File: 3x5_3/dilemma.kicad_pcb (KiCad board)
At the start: 2 copper layers, 134.1 x 215.6 mm, 91 parts, among them J5001 BATTERY_CONN_DEANS, J5011 BATTERY_CONN_DEANS, SW101 NA_SW_Push, SW102 NA_SW_Push, SW103 NA_SW_Push, SW104 NA_SW_Push, SW105 NA_SW_Push, SW106 NA_SW_Push, SW107 NA_SW_Push, SW108 NA_SW_Push, SW109 NA_SW_Push, SW112 NA_SW_Push, SW113 NA_SW_Push, SW114 NA_SW_Push, SW115 NA_SW_Push, SW116 NA_SW_Push, SW117 NA_SW_Push, SW118 NA_SW_Push, SW119 NA_SW_Push, SW3001 NA_SW_Push, SW5002 NA_SW_Push, SW5003 NA_SW_Push, SW5004 NA_SW_Push, SW5005 NA_SW_Push, SW5006 NA_SW_Push, SW5007 NA_SW_Push, SW5008 NA_SW_Push, SW5009 NA_SW_Push, SW5010 NA_SW_Push, SW5011 NA_SW_Push, SW5012 NA_SW_Push, SW5013 NA_SW_Push, SW5014 NA_SW_Push, SW5015 NA_SW_Push, SW5016 NA_SW_Push, SW5017 NA_SW_Push, SW5018 NA_SW_Push, SW5019 NA_SW_Push, SW5021 SW_SPST, SW5022 SW_SPST, U5001 eliteC, U5007 eliteC

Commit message: add right side edge cuts
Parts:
- removed H101, H102, H104, H108: NA_M4, local-libraries:MountingHole_3mm_Pad_Via
- removed H111: NA_Mount, local-libraries:Tenting_Puck
- SW101, SW102, SW103, SW104, SW105, SW106, SW107, SW108, SW109, SW112, SW113, SW114, SW115, SW116, SW117, SW118, SW119, SW3001, SW5002, SW5003, SW5004, SW5005, SW5006, SW5007, SW5008, SW5009, SW5010, SW5011, SW5012, SW5013, SW5014, SW5015, SW5016, SW5017, SW5018, SW5019: footprint local-libraries:SW_Kailh_Choc_V2_1.00u -> local-libraries:SW_Kailh_Choc_V1V2_1.00u
- moved D115 152.3 mm to (59.8, 42.8), turned to 0 degrees
- moved D5038 148.0 mm to (65.6, 46.2), turned to 0 degrees
- moved D5034 143.9 mm to (59.8, 56.2), turned to 0 degrees
- moved D5046 135.7 mm to (71.4, 49.5), turned to 0 degrees
- moved D5045 134.7 mm to (71.4, 46.2), turned to 0 degrees
- moved D5044 118.1 mm to (71.4, 42.8), turned to 0 degrees
- moved D5043 115.8 mm to (71.4, 39.5), turned to 0 degrees
- moved D5042 115.0 mm to (65.6, 59.6), turned to 0 degrees
- moved D5039 103.6 mm to (65.6, 49.5), turned to 0 degrees
- moved D5041 103.3 mm to (65.6, 56.2), turned to 0 degrees
- moved D5040 102.7 mm to (65.6, 52.9), turned to 0 degrees
- moved D5035 90.3 mm to (59.8, 59.6), turned to 0 degrees
- moved D5037 89.5 mm to (65.6, 42.8), turned to 0 degrees
- moved D5033 77.0 mm to (59.8, 52.9), turned to 0 degrees
- moved D5032 75.6 mm to (59.8, 49.5), turned to 0 degrees
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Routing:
- net M_COL1: track 168.1 -> 0.00 mm, vias 1 -> 0
- net M_COL3: track 159.6 -> 0.00 mm, vias 1 -> 0
- net M_COL2: track 143.8 -> 0.00 mm, vias 1 -> 0
- net M_ROW4: track 137.9 -> 0.00 mm
- net M_ROW2: track 120.6 -> 0.00 mm
- net M_ROW1: track 113.2 -> 0.00 mm
- net M_ROW3: track 109.2 -> 0.00 mm
- net M_COL5: track 76.5 -> 0.00 mm, vias 1 -> 0
- net M_COL4: track 74.1 -> 0.00 mm, vias 1 -> 0
- net BAT: track 67.9 -> 0.00 mm
- net BAT_SW: track 30.1 -> 0.00 mm
- net Net-(D5041-A): track 22.4 -> 0.00 mm
- net Net-(D5032-A): track 20.6 -> 0.00 mm
- net Net-(D115-A): track 20.5 -> 0.00 mm
- net Net-(D112-A): track 20.4 -> 0.00 mm
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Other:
- board size 134.1 x 215.6 mm -> 273.1 x 220.6 mm

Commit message: left half edge cuts
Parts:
- removed D5001, D5002, D5003, D5004, D5005, D5006, D5007, D5008, D5009, D5010, D5011, D5012, D5013, D5014, D5015, D5016, D5017, D5018: D, Diode_SMD:D_SOD-123
- removed H5001, H5002, H5003, H5007: NA_M4, local-libraries:MountingHole_3mm_Pad_Via
- removed H5008: NA_Mount, local-libraries:Tenting_Puck
- moved D5038 153.4 mm to (203.7, 112.9), turned to 150 degrees
- moved D115 143.1 mm to (196.2, 85.9), turned to 180 degrees
- moved D5034 134.2 mm to (184.7, 105.2), turned to 165 degrees
- moved D5046 126.3 mm to (196.5, 66.7), turned to 180 degrees
- moved D5045 125.1 mm to (196.5, 47.7), turned to 180 degrees
- moved D5042 108.9 mm to (165.5, 102.9), turned to 180 degrees
- moved D5044 108.2 mm to (177.4, 64.4), turned to 180 degrees
- moved D5043 106.0 mm to (177.2, 45.2), turned to 180 degrees
- moved D5041 95.4 mm to (158.2, 78.9), turned to 180 degrees
- moved D5039 93.1 mm to (158.2, 40.7), turned to 180 degrees
- moved D5040 92.9 mm to (158.2, 59.7), turned to 180 degrees
- moved D5037 84.8 mm to (139.2, 84.9), turned to 180 degrees
- moved D5035 80.5 mm to (139.2, 46.7), turned to 180 degrees
- moved D5033 74.8 mm to (120.2, 96.9), turned to 180 degrees
- moved D5032 66.7 mm to (120.2, 77.7), turned to 180 degrees
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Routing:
- net M_COL1_L: track 169.1 -> 0.00 mm, vias 1 -> 0
- net M_COL3_L: track 158.7 -> 0.00 mm, vias 1 -> 0
- net M_COL2_L: track 146.2 -> 0.00 mm, vias 1 -> 0
- net M_ROW2: track 0.00 -> 88.3 mm
- net M_ROW4: track 0.00 -> 88.3 mm
- net M_ROW3: track 0.00 -> 88.3 mm
- net M_COL1: track 0.00 -> 83.3 mm
- net M_COL2: track 0.00 -> 75.8 mm
- net M_COL5_L: track 74.9 -> 0.38 mm, vias 1 -> 0
- net M_COL4_L: track 73.9 -> 0.00 mm, vias 1 -> 0
- net M_COL3: track 0.00 -> 72.9 mm
- net M_ROW1_L: track 114.7 -> 48.6 mm
- net RESET_L: track 60.4 -> 0.00 mm, vias 1 -> 0
- net M_ROW4_L: track 137.4 -> 86.4 mm
- net M_ROW1: track 0.00 -> 48.6 mm
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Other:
- board size 273.1 x 220.6 mm -> 134.1 x 215.7 mm

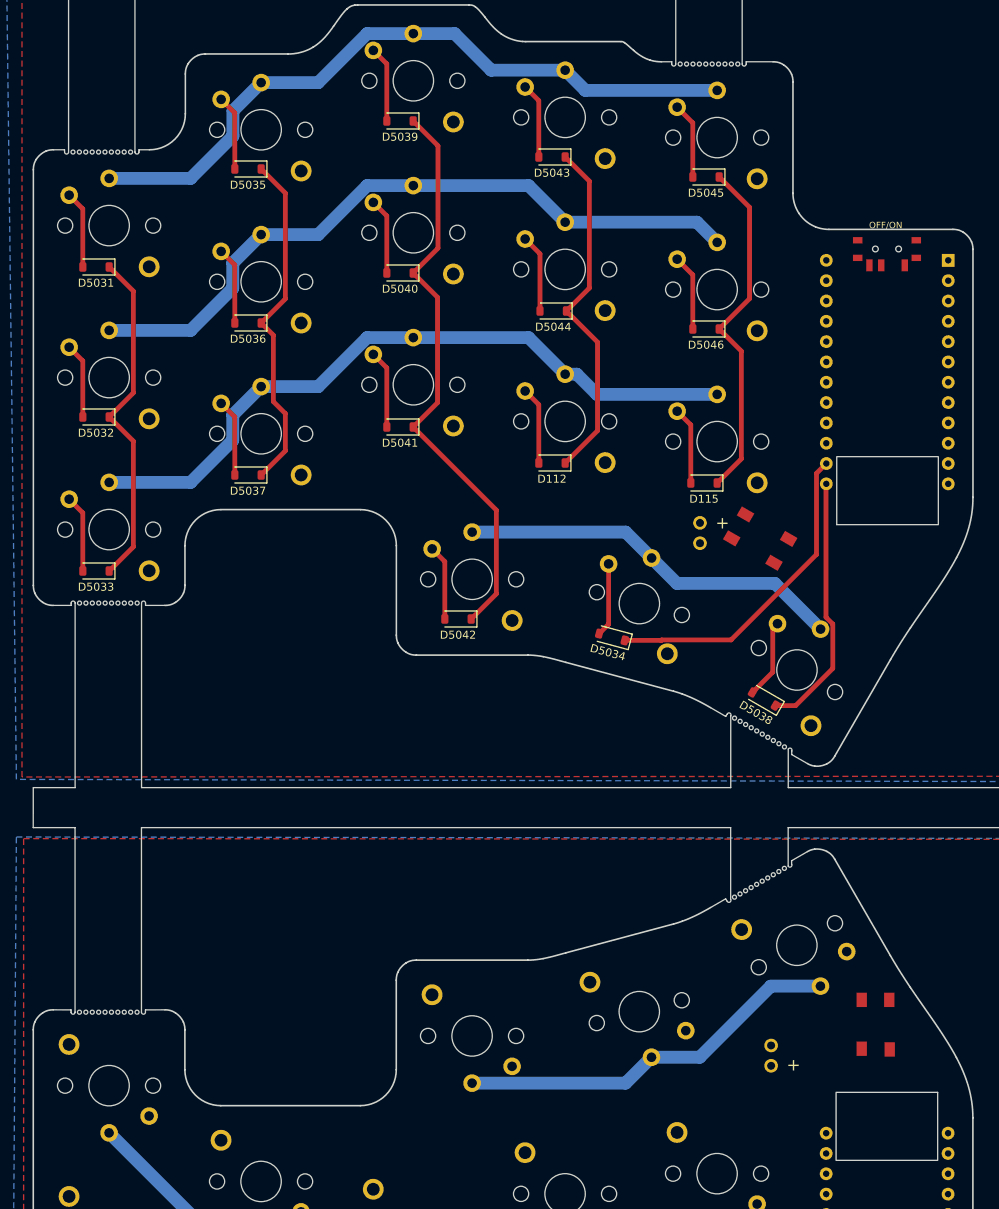
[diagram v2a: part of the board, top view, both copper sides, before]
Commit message: routed right matrix
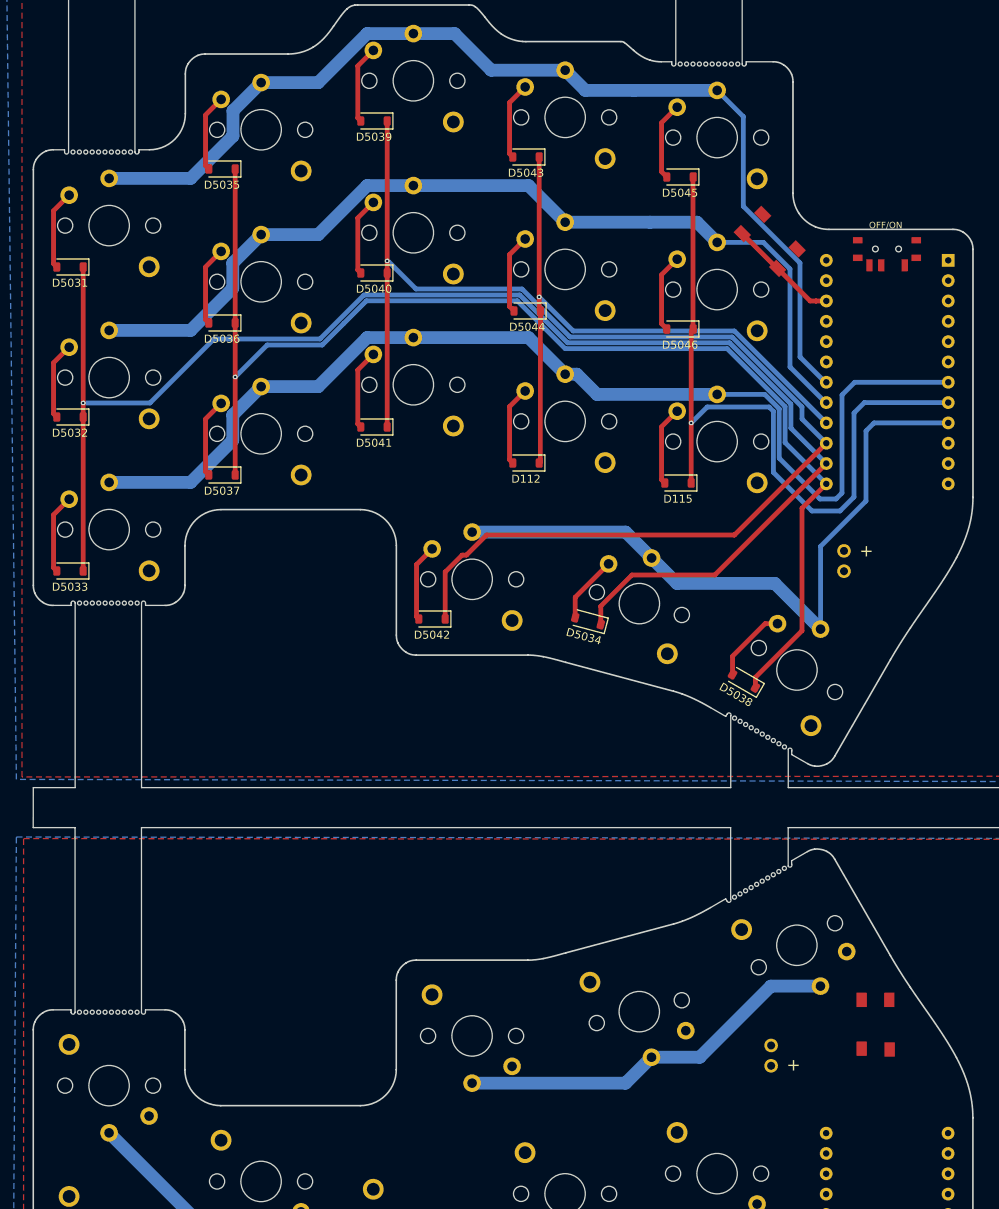
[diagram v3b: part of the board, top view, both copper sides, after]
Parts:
- moved SW5022 37.3 mm to (204.5, 55.7), turned to 135 degrees
- moved J5011 18.3 mm to (213.7, 96.9)
- moved D5034 3.61 mm to (181.7, 103.2)
- moved D5038 3.36 mm to (201.2, 110.7)
- moved D112 3.25 mm to (174.0, 83.4)
- moved D115 3.25 mm to (193.0, 85.9)
- moved D5031 3.25 mm to (117.0, 58.9)
- moved D5032 3.25 mm to (117.0, 77.7)
- moved D5033 3.25 mm to (117.0, 96.9)
- moved D5035 3.25 mm to (136.0, 46.7)
- moved D5036 3.25 mm to (136.0, 65.9)
- moved D5037 3.25 mm to (136.0, 84.9)
- moved D5039 3.25 mm to (155.0, 40.7)
- moved D5040 3.25 mm to (155.0, 59.7)
- moved D5041 3.25 mm to (155.0, 78.9)
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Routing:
- net M_COL1: track 83.3 -> 184.8 mm, vias 0 -> 1
- net M_COL3: track 72.9 -> 163.6 mm, vias 0 -> 1
- net M_COL2: track 75.8 -> 157.3 mm, vias 0 -> 1
- net M_ROW4: track 88.3 -> 139.4 mm
- net M_COL5: track 43.8 -> 93.0 mm, vias 0 -> 1
- net M_ROW2: track 88.3 -> 130.5 mm
- net M_ROW1: track 48.6 -> 86.4 mm
- net M_COL4: track 44.0 -> 80.8 mm, vias 0 -> 1
- net M_ROW3: track 88.3 -> 117.4 mm
- net RESET: track 0.00 -> 14.0 mm
- net Net-(D5034-A): track 9.20 -> 8.44 mm

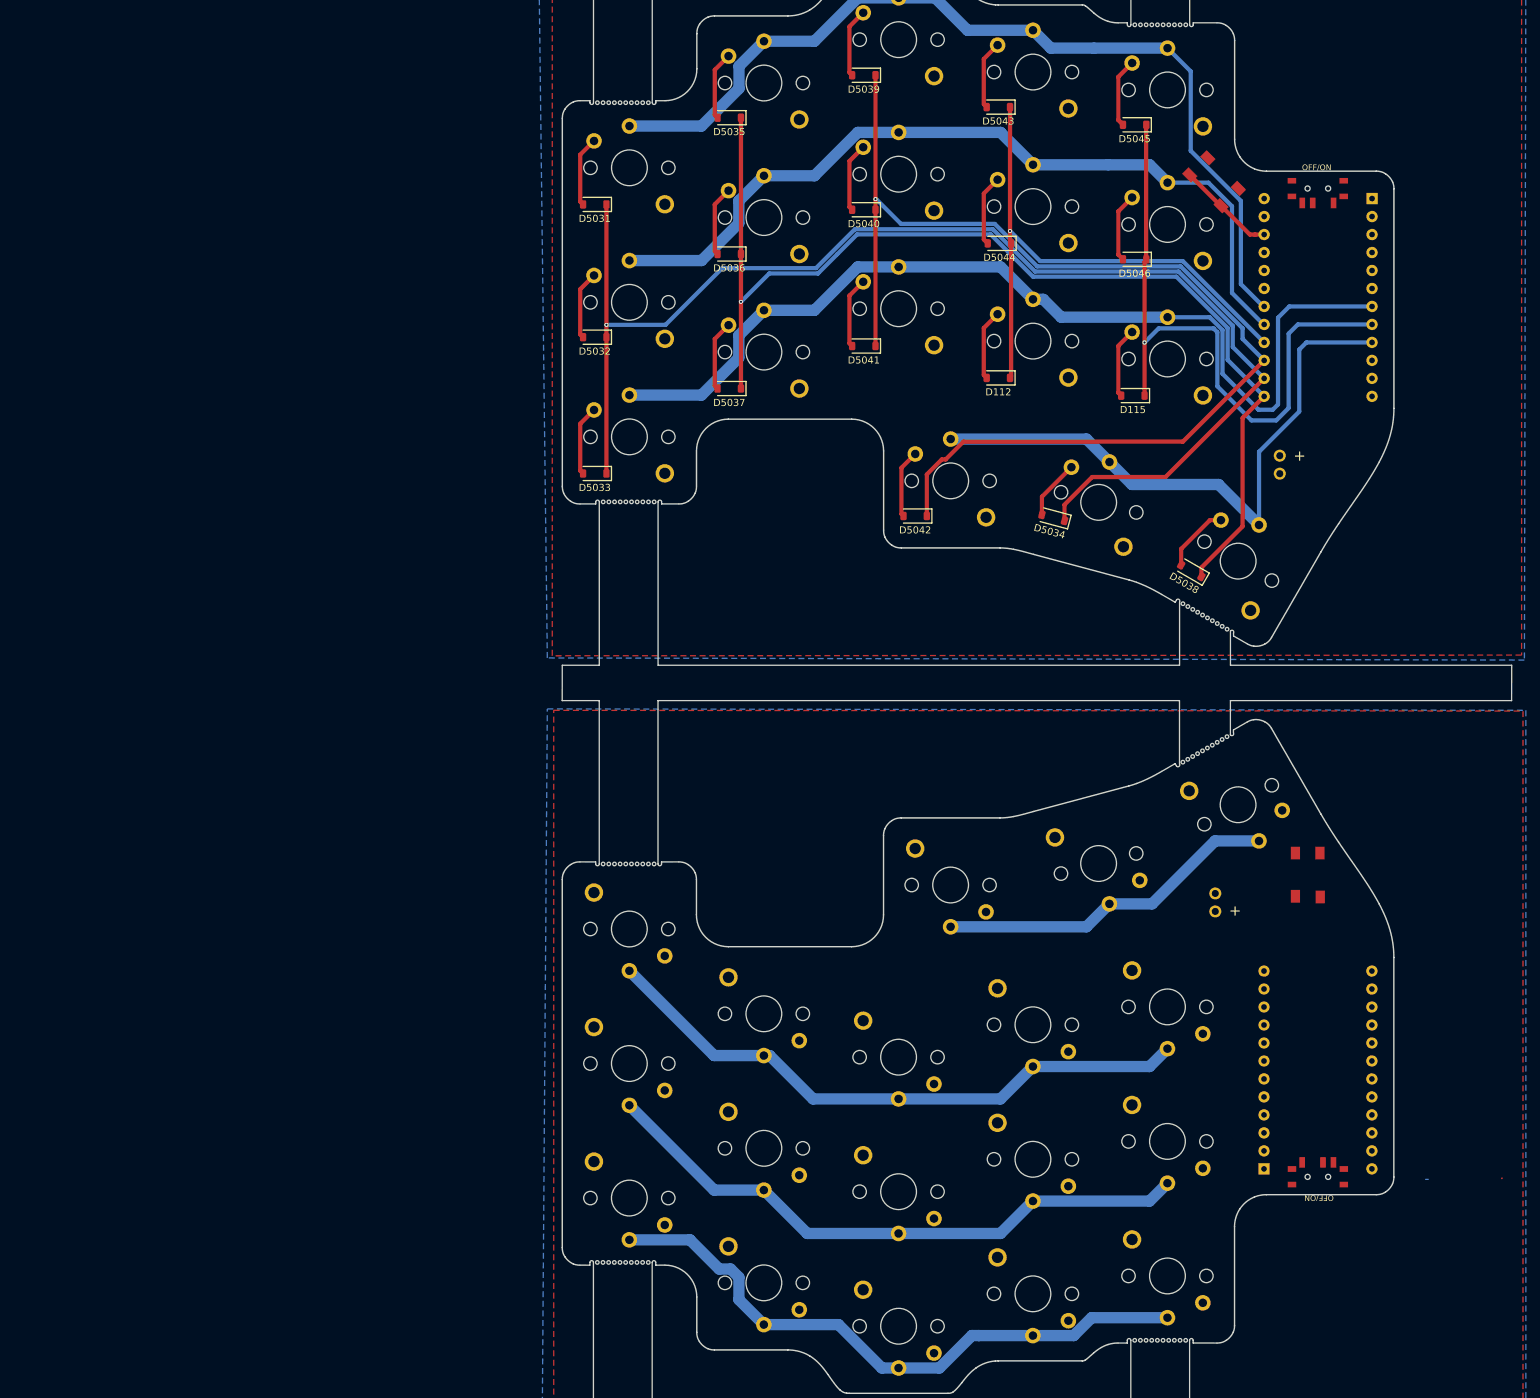
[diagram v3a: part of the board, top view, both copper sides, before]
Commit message: routed left matrix
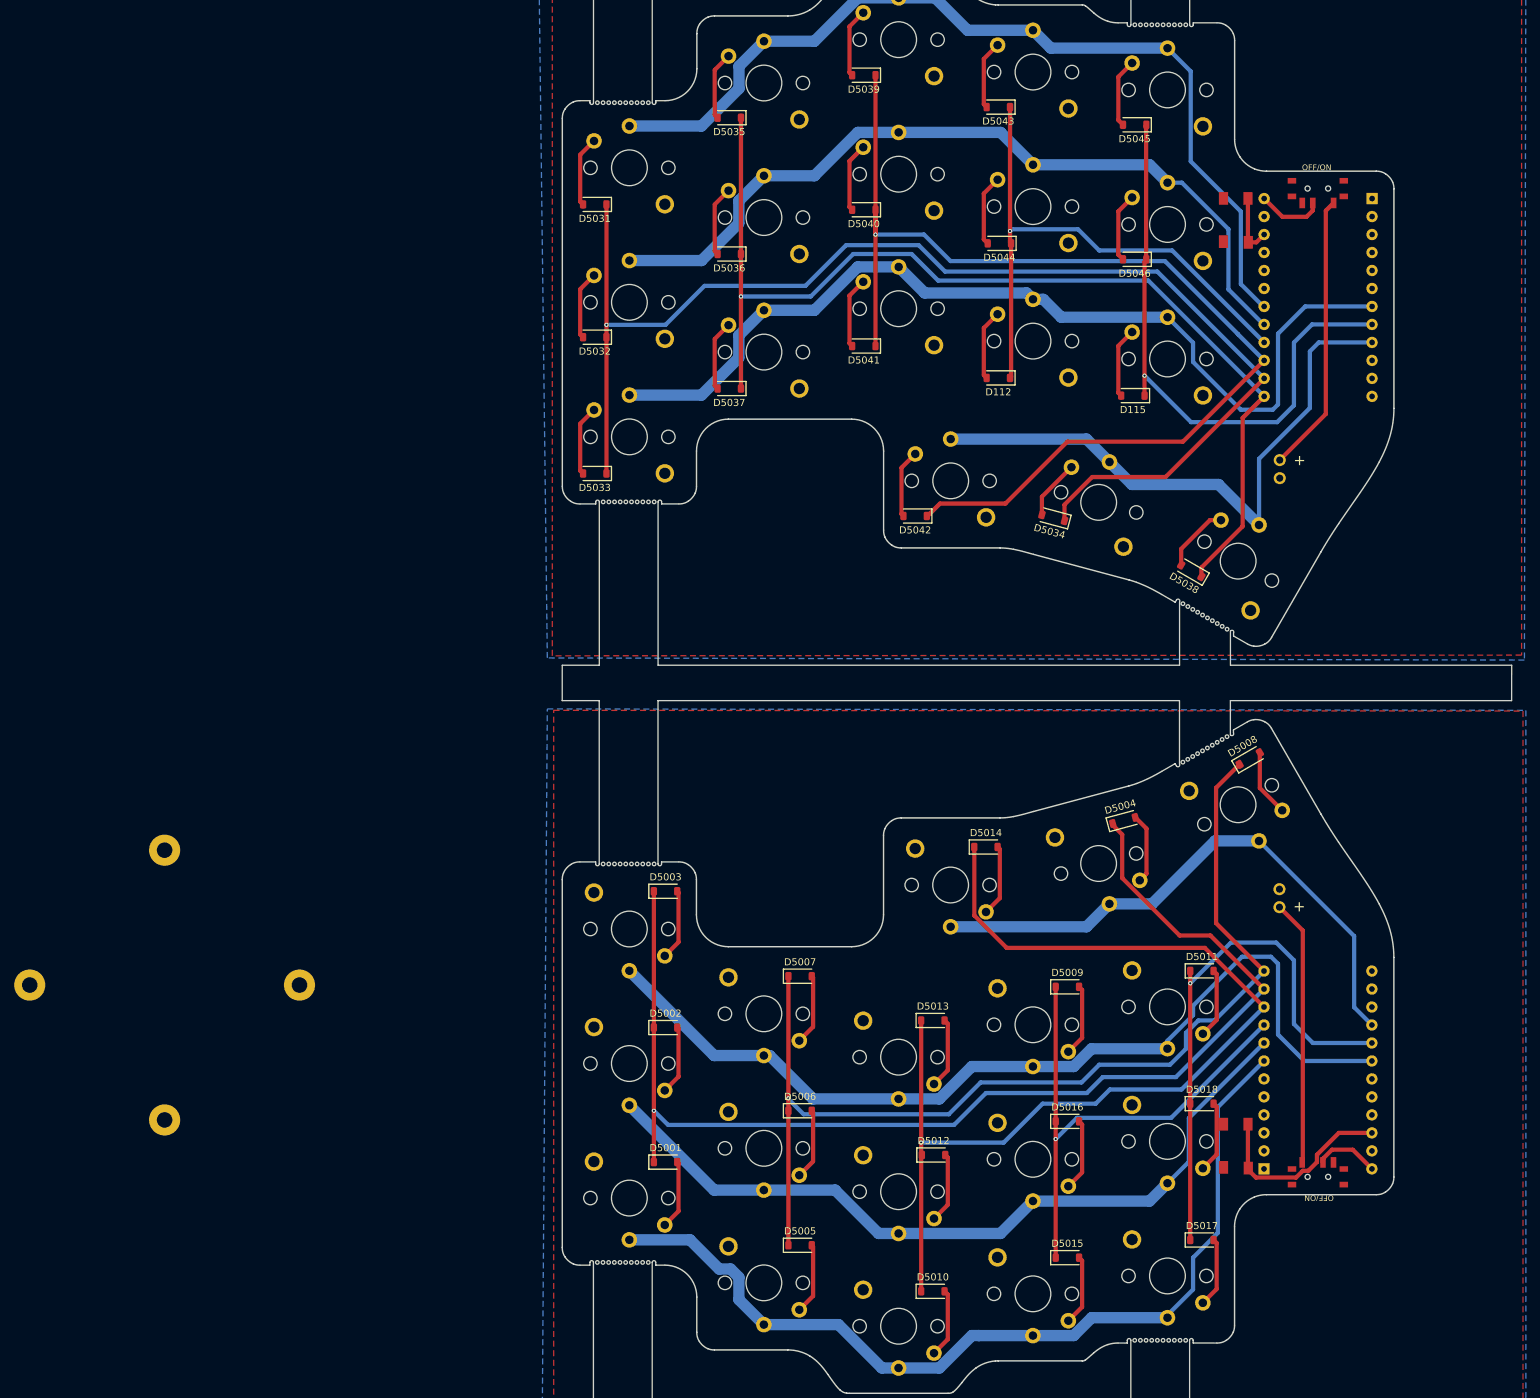
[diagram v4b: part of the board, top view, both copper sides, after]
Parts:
- added D5001: D, Diode_SMD:D_SOD-123, F.Cu at (127.0, 194.2)
- added D5002: D, Diode_SMD:D_SOD-123, F.Cu at (127.0, 175.2)
- added D5003: D, Diode_SMD:D_SOD-123, F.Cu at (127.0, 155.9)
- added D5004: D, Diode_SMD:D_SOD-123, F.Cu at (191.7, 145.9)
- added D5005: D, Diode_SMD:D_SOD-123, F.Cu at (146.0, 205.9)
- added D5006: D, Diode_SMD:D_SOD-123, F.Cu at (146.0, 186.9)
- added D5007: D, Diode_SMD:D_SOD-123, F.Cu at (146.0, 167.9)
- added D5008: D, Diode_SMD:D_SOD-123, F.Cu at (209.5, 137.2)
- added D5009: D, Diode_SMD:D_SOD-123, F.Cu at (183.7, 169.4)
- added D5010: D, Diode_SMD:D_SOD-123, F.Cu at (164.7, 212.4)
- added D5011: D, Diode_SMD:D_SOD-123, F.Cu at (202.7, 167.2)
- added D5012: D, Diode_SMD:D_SOD-123, F.Cu at (164.8, 193.2)
- added D5013: D, Diode_SMD:D_SOD-123, F.Cu at (164.7, 174.2)
- added D5014: D, Diode_SMD:D_SOD-123, F.Cu at (172.2, 149.7)
- added D5015: D, Diode_SMD:D_SOD-123, F.Cu at (183.7, 207.7)
- added D5016: D, Diode_SMD:D_SOD-123, F.Cu at (183.7, 188.4)
- added D5017: D, Diode_SMD:D_SOD-123, F.Cu at (202.7, 205.2)
- added D5018: D, Diode_SMD:D_SOD-123, F.Cu at (202.7, 185.9)
- added H5008: NA_Mount, local-libraries:Tenting_Puck, F.Cu at (56.2, 169.2)
- moved SW5021 39.6 mm to (207.5, 191.9)
- moved J5001 9.08 mm to (213.7, 155.6)
- moved SW5022 6.26 mm to (207.5, 61.2), turned to -90 degrees
- moved J5011 0.63 mm to (213.7, 97.6)
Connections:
- PSW5001 pad 1: BAT -> BAT_SW
- PSW5001 pad 2: BAT_SW -> BAT
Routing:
- net M_COL1_L: track 0.00 -> 168.0 mm, vias 0 -> 1
- net M_COL3_L: track 0.00 -> 150.6 mm, vias 0 -> 1
- net M_COL2_L: track 0.00 -> 149.2 mm, vias 0 -> 1
- net M_COL5_L: track 0.38 -> 77.2 mm, vias 0 -> 1
- net M_COL4_L: track 0.00 -> 74.3 mm, vias 0 -> 1
- net M_ROW4_L: track 86.4 -> 134.1 mm
- net M_ROW2_L: track 88.3 -> 130.2 mm
- net BAT_SW: track 0.00 -> 39.5 mm
- net BAT_SW_L: track 0.03 -> 37.5 mm
- net M_ROW1_L: track 48.6 -> 81.2 mm
- net RESET_L: track 0.00 -> 27.6 mm
- net M_ROW3_L: track 86.4 -> 111.9 mm
- net Net-(D5016-A): track 0.00 -> 10.1 mm
- net Net-(D5009-A): track 0.00 -> 10.1 mm
- net Net-(D5018-A): track 0.00 -> 10.1 mm
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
